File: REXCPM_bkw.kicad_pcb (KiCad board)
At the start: 2 copper layers, 38 x 16.6 mm, 18 parts, among them J1 Tandy_100_102_200_option_rom, J2 Conn_01x03_Pin, U1 XCR3064XL, U2 CY61277, U3 4245, U4 4245, U5 NCV563SQ33, U6 NCV563SQ33

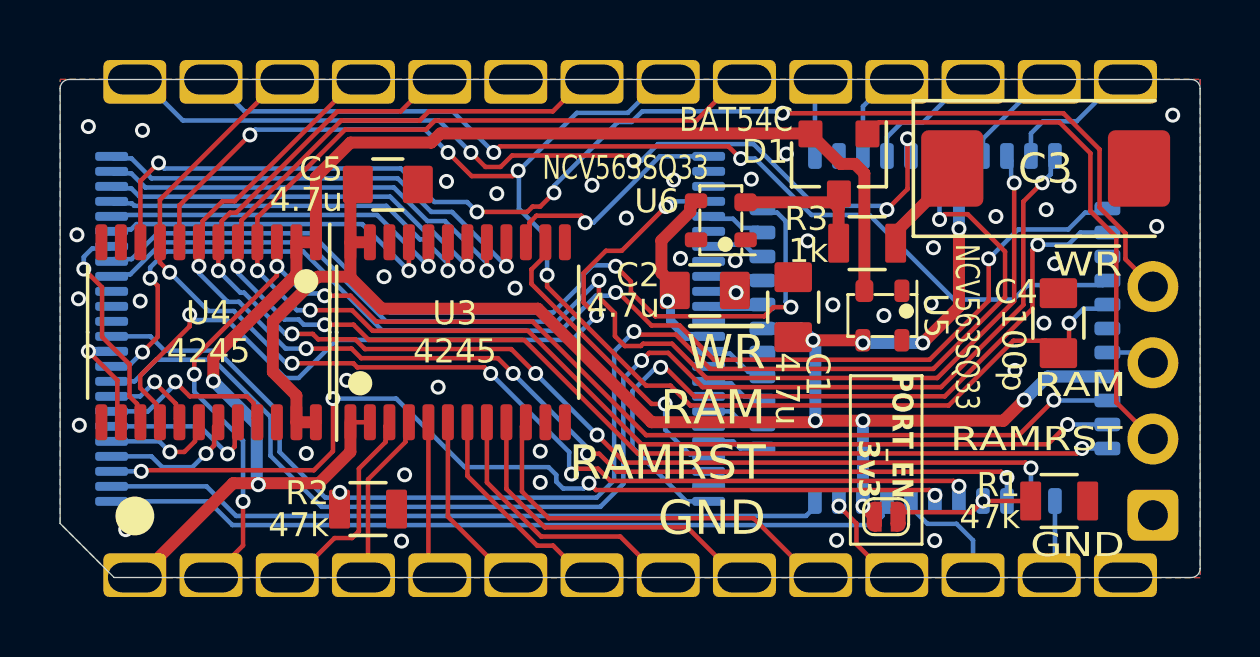
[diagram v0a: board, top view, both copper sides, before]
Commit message: streamline rexcpm routing
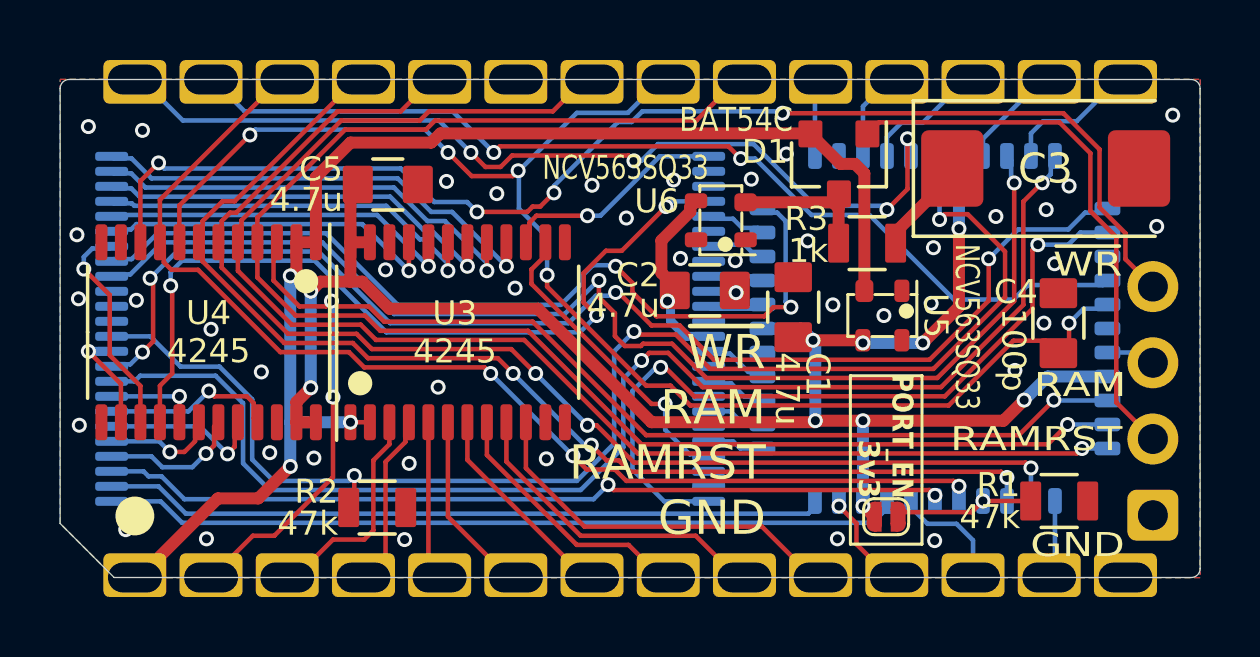
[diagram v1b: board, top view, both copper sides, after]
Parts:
- moved R2 0.31 mm to (128.8, 105.2)
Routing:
- net VBUS: track 46.2 -> 42.7 mm, vias 2 -> 3
- net /SRAM_A13: track 31.3 -> 28.4 mm, vias 4 -> 2
- net /SRAM_A19: track 44.7 -> 43.5 mm
- net /SRAM_OE: track 26.6 -> 27.5 mm
- net +3V3: track 58.2 -> 57.5 mm, vias 8 -> 10
- net /BUS_A10: track 43.9 -> 43.2 mm, vias 5 -> 3
- net /BUS_A0: track 13.5 -> 12.9 mm
- net /BUS_A8: track 38.7 -> 38.1 mm, vias 5 -> 3
- net /SRAM_A20: track 41.9 -> 41.4 mm
- net /BUS_A2: track 9.36 -> 8.83 mm
- net /BUS_A1: track 11.4 -> 10.8 mm
- net /SRAM_CS2: track 46.6 -> 46.1 mm
- net /BUS_A9: track 39.8 -> 39.3 mm, vias 5 -> 3
- net /BUS_A11: track 50.9 -> 51.1 mm, vias 3 -> 1
- net /BUS_A12: track 41.8 -> 41.7 mm, vias 5 -> 3
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
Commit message: rexcpm small layout opts
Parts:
- U2: value CY61277 -> RMLV3216AGSA
- moved JP1 0.71 mm to (146.2, 106.0)
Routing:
- net +3V3: track 57.5 -> 58.3 mm
- net GND: vias 44 -> 42

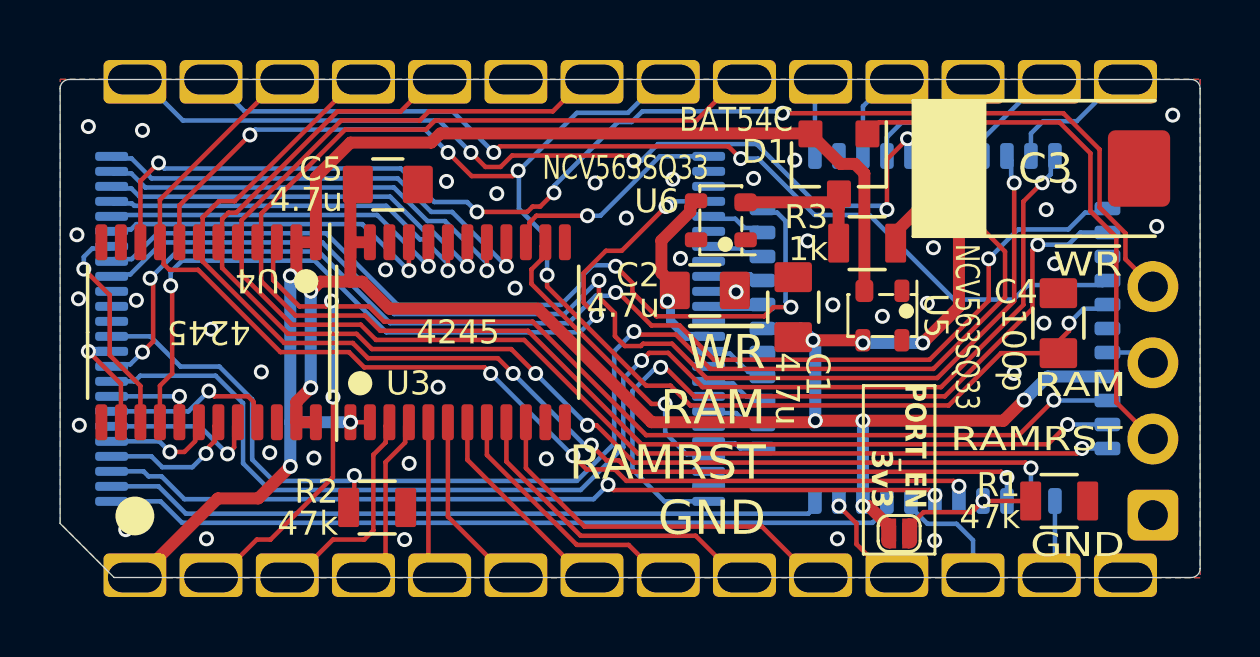
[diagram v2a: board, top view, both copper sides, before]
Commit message: rexcpm qwiic connector
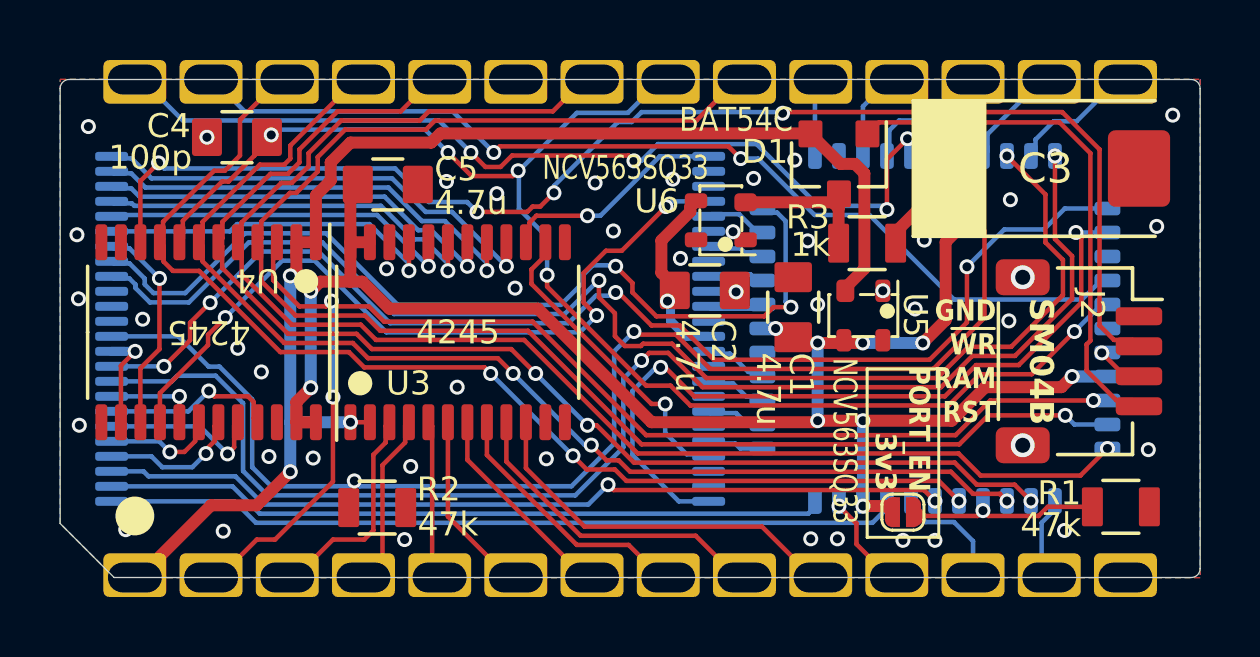
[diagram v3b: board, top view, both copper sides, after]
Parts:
- J2: value Conn_01x03_Pin -> SM04B; footprint 000_LOCAL:PinHeader_1x04_P2.54mm_Horizontal -> 000_LOCAL:JST_SH_SM04B-SRSS-TB_1x04-1MP_P1.00mm_Horizontal
- moved C4 28.1 mm to (124.1, 92.8), turned to 180 degrees
- moved J2 5.69 mm to (152.2, 100.3), turned to -90 degrees
- moved R1 2.07 mm to (153.6, 105.1)
- moved JP1 0.72 mm to (146.3, 105.3)
- moved U5 0.63 mm to (145.0, 98.8)
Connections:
- J2 pad 2: /RAM_RST -> /~{BUS_WR}
- J2 pad 4: /~{BUS_WR} -> /RAM_RST
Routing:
- net /SRAM_A18: track 40.2 -> 43.2 mm
- net /PORT_EN: track 5.06 -> 7.25 mm
- net /~{BUS_WR}: track 42.3 -> 44.5 mm
- net /SRAM_OE: track 27.5 -> 25.5 mm
- net /SRAM_A19: track 43.5 -> 45.1 mm
- net +3V3: track 58.3 -> 57.3 mm, vias 10 -> 11
- net /SRAM_A17: track 29.6 -> 30.6 mm
- net /RAM_RST: track 18.4 -> 17.5 mm
- net /BUS_A13: track 46.9 -> 47.8 mm
- net /~{BUS_OE}: track 46.9 -> 46.1 mm
- net /SRAM_A20: track 41.4 -> 40.6 mm
- net VBUS: track 42.7 -> 43.4 mm
- net /RAM: track 1.66 -> 1.56 mm, vias 0 -> 1
- net GND: vias 42 -> 46
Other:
- board text added: "GND ~{WR} RAM RST"
- board text removed: "RAM"
- board text removed: "RAMRST"
- board text removed: "~{WR}"
- board text removed: "~{WR} RAM RAMRST GND"

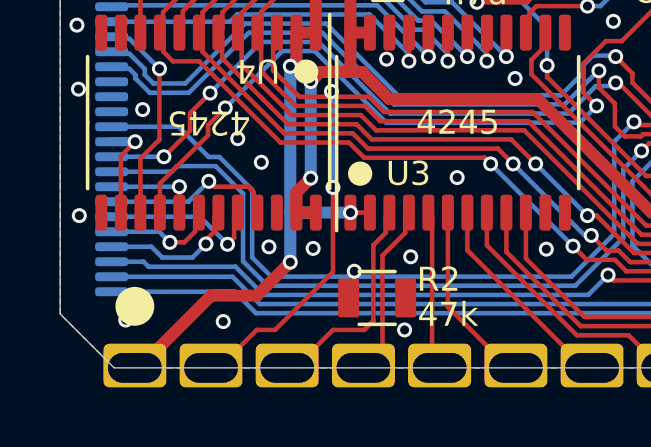
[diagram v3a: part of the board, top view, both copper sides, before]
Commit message: rexcpm add cap on vbus
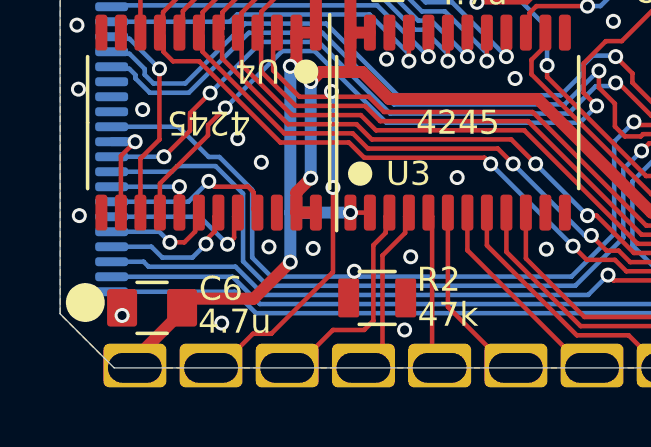
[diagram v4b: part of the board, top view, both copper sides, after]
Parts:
- added C6: 4.7u, 000_LOCAL:C_0805, F.Cu at (121.3, 105.5)
